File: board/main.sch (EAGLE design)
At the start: 62 parts, among them IC1 W65C02S6TP

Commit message: updated schematic
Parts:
- added IC6: (no value), memory-hitachi:62256P
- added IC7: 74LS00N, 74xx-eu:74LS00N
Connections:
- new net N$58: IC6.!CS, IC7A.O
- new net _A15: IC7A.I1, IC7C.O
- net A0: now also IC6.A0
- net A1: now also IC6.A1
- net A10: now also IC6.A10
- net A11: now also IC6.A11
- net A12: now also IC6.A12
- net A13: now also IC6.A13
- net A14: now also IC6.!OE, IC6.A14
- net A15: now also IC7C.I0, IC7C.I1
- net A2: now also IC6.A2
- net A3: now also IC6.A3
- net A4: now also IC6.A4
- net A5: now also IC6.A5
- net A6: now also IC6.A6
- net A7: now also IC6.A7
- net A8: now also IC6.A8
- net A9: now also IC6.A9
- net CLOCK: now also IC7A.I0
- net D0: now also IC6.I/O0
- net D1: now also IC6.I/O1
- net D2: now also IC6.I/O2
- net D3: now also IC6.I/O3
- net D4: now also IC6.I/O4
- net D5: now also IC6.I/O5
- net D6: now also IC6.I/O6
- net D7: now also IC6.I/O7
- net GND: now also IC6.VSS
- net R/_W: now also IC6.!WE
- net VCC: now also IC6.VCC

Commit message: modified board
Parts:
- added D1, D2: 1N4148DO35-7, diode:1N4148DO35-7
- added D3: 3.9v, diode:ZENER-DIODEDO34-7
- added IC7-ROM: AT28C256-28DIP, atmel-custom:AT28C256-28DIP
- added LED27, LED28: (no value), led:LED5MM
- added Q1: BC327, transistor-pnp:BC327
- added R30, R31: 220Ω, rcl:R-EU_0207/10
- added R32, R33, R34: 220kΩ, rcl:R-EU_0207/10
- added T1: BC337, transistor:BC337
- added U$1: W65C22S6TP, 6502:W65C22S6TP
- renumbered IC6 to IC6-RAM
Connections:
- removed net R/_W: IC11.R!WB, IC5.I7, IC6-RAM.!WE
- removed net _A15: IC7A.I1, IC7C.O
- removed net _RES: C1.1, IC11.!RESB, R1.1, R2.2, S1.P, S1.P1
- new net A14*: IC7A.O, IC7D.I0
- new net A15*: IC7-ROM./OE, IC7C.O, IC7D.I1
- new net CLOCK*: D2.A, IC7-ROM./CE, IC7B.O
- new net CS_RAM: D1.A, IC7D.O, R33.1
- new net N$54: LED27.A, R30.2
- new net N$55: Q1.C, R31.1
- new net N$56: LED28.A, R31.2
- new net N$57: D1.C, D2.C, IC6-RAM.!CS, R32.1
- new net N$59: D3.A, Q1.B
- new net N$60: R34.2, T1.B
- new net N$61: D3.C, R33.2
- new net PB0: U$1VIA.PB0
- new net PB1: U$1VIA.PB1
- new net PB2: U$1VIA.PB2
- new net PB3: U$1VIA.PB3
- new net PB4: U$1VIA.PB4
- new net PB5: U$1VIA.PB5
- new net PB6: U$1VIA.PB6
- new net PB7: U$1VIA.PB7
- new net R/W*: IC11.R!WB, IC5.I7, IC6-RAM.!WE, U$1VIA.R!WB
- new net RES*: C1.1, IC11.!RESB, R1.1, R2.2, S1.P, S1.P1, U$1VIA.!RESB
- net A0: now also IC7-ROM.A0, U$1VIA.RS0
- net A1: now also IC7-ROM.A1, U$1VIA.RS1
- net A10: now also IC7-ROM.A10
- net A11: now also IC7-ROM.A11
- net A12: now also IC7-ROM.A12
- net A13: now also IC7-ROM.A13
- net A14: now also IC7-ROM.A14, IC7A.I0, IC7A.I1, U$1VIA.CS1
- net A15: now also R34.1, U$1VIA.!CS2B
- net A2: now also IC7-ROM.A2, U$1VIA.RS2
- net A3: now also IC7-ROM.A3, U$1VIA.RS3
- net A4: now also IC7-ROM.A4
- net A5: now also IC7-ROM.A5
- net A6: now also IC7-ROM.A6
- net A7: now also IC7-ROM.A7
- net A8: now also IC7-ROM.A8
- net A9: now also IC7-ROM.A9
- net CLOCK: now also IC7B.I0, IC7B.I1, U$1VIA.PHI2; no longer IC7A.I0
- net D0: now also IC7-ROM.I/O0, U$1VIA.D0
- net D1: now also IC7-ROM.I/O1, U$1VIA.D1
- net D2: now also IC7-ROM.I/O2, U$1VIA.D2
- net D3: now also IC7-ROM.I/O3, U$1VIA.D3
- net D4: now also IC7-ROM.I/O4, U$1VIA.D4
- net D5: now also IC7-ROM.I/O5, U$1VIA.D5
- net D6: now also IC7-ROM.I/O6, U$1VIA.D6
- net D7: now also IC7-ROM.I/O7, U$1VIA.D7
- net GND: now also IC7-ROM.GND, IC7P.GND, LED28.C, R32.2, T1.E, U$1VIAP.VSS
- net N$58: now also LED27.C, T1.C; no longer IC6-RAM.!CS, IC7A.O
- net VCC: now also IC7-ROM./WE, IC7-ROM.VCC, IC7P.VCC, Q1.E, R30.1, U$1VIA.!IRQB, U$1VIAP.VDD
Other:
- note added: "CY62256"
- moved on the sheet: IC7A, IC7C

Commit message: modified board
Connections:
- net A15*: now also IC7-ROM./CE; no longer IC7-ROM./OE
- net CLOCK*: no longer IC7-ROM./CE
- net GND: now also IC7-ROM./OE
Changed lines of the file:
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@@
 <part name="GND15" library="supply1" library_urn="urn:adsk.eagle:library:371" deviceset="GND" device=""/>
 <part name="P+13" library="supply1" library_urn="urn:adsk.eagle:library:371" deviceset="VCC" device=""/>
+<part name="GND16" library="supply1" library_urn="urn:adsk.eagle:library:371" deviceset="GND" device=""/>
 </parts>
 <sheets>
@@
 <instance part="P+13" gate="VCC" x="421.64" y="68.58" smashed="yes">
 <attribute name="VALUE" x="419.1" y="66.04" size="1.778" layer="96" rot="R90"/>
+</instance>
+<instance part="GND16" gate="1" x="340.36" y="45.72" smashed="yes">
+<attribute name="VALUE" x="337.82" y="43.18" size="1.778" layer="96"/>
 </instance>
 </instances>
@@
 <pinref part="GND15" gate="1" pin="GND"/>
 </segment>
+<segment>
+<pinref part="IC7-ROM" gate="G$1" pin="/OE"/>
+<wire x1="330.2" y1="50.8" x2="340.36" y2="50.8" width="0.1524" layer="91"/>
+<wire x1="340.36" y1="50.8" x2="340.36" y2="48.26" width="0.1524" layer="91"/>
+<pinref part="GND16" gate="1" pin="GND"/>
+</segment>
 </net>
 <net name="RES*" class="0">
@@
 </segment>
 <segment>
-<pinref part="IC7-ROM" gate="G$1" pin="/OE"/>
-<wire x1="330.2" y1="50.8" x2="332.74" y2="50.8" width="0.1524" layer="91"/>
-<label x="332.74" y="50.8" size="1.27" layer="95" xref="yes"/>
+<label x="332.74" y="48.26" size="1.27" layer="95" xref="yes"/>
+<pinref part="IC7-ROM" gate="G$1" pin="/CE"/>
+<wire x1="332.74" y1="48.26" x2="330.2" y2="48.26" width="0.1524" layer="91"/>
 </segment>
 </net>
@@
 </segment>
 <segment>
-<pinref part="IC7-ROM" gate="G$1" pin="/CE"/>
-<wire x1="330.2" y1="48.26" x2="332.74" y2="48.26" width="0.1524" layer="91"/>
-<label x="332.74" y="48.26" size="1.27" layer="95" xref="yes"/>
-</segment>
-<segment>

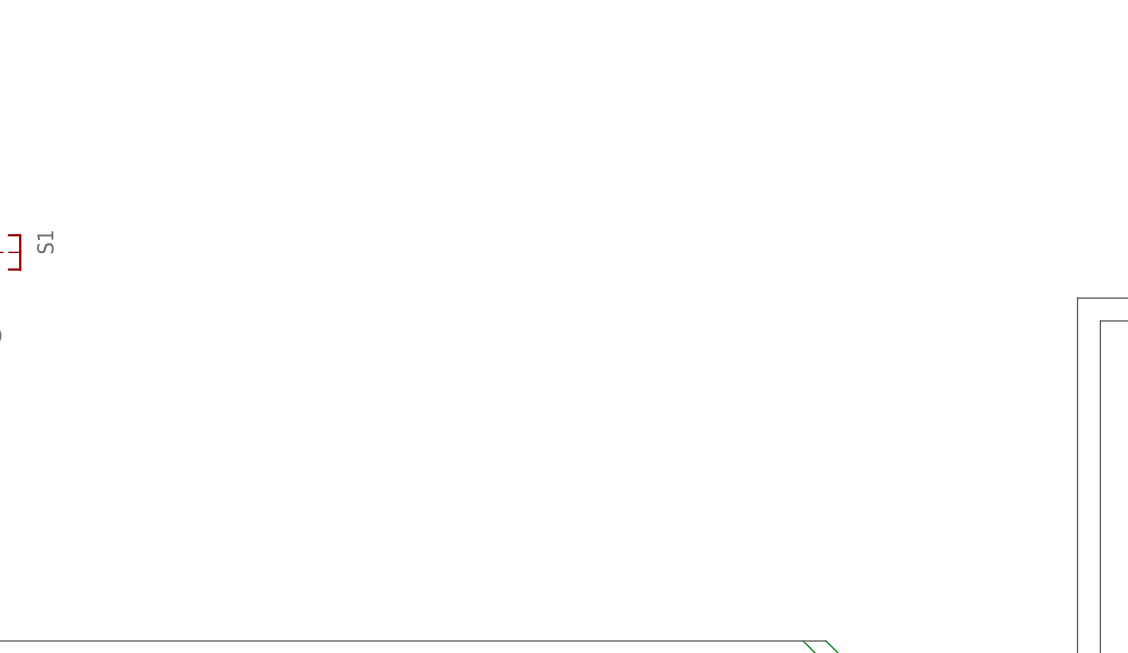
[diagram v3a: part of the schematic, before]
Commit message: added 555 circuit
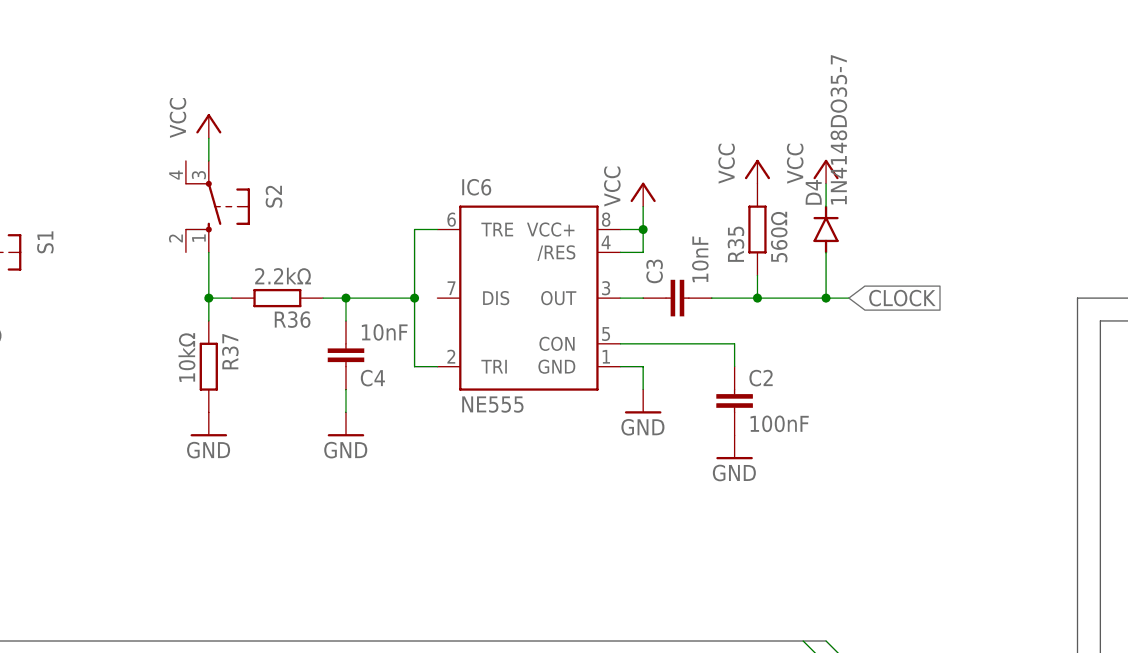
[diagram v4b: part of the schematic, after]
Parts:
- added C2: 100nF, rcl:C-EU050-025X075
- added C3, C4: 10nF, rcl:C-EU050-025X075
- added D4: 1N4148DO35-7, diode:1N4148DO35-7
- added IC6: NE555, st-microelectronics:NE555
- added R35: 560Ω, rcl:R-EU_0207/10
- added R36: 2.2kΩ, rcl:R-EU_0207/10
- added R37: 10kΩ, rcl:R-EU_0207/10
- added S2: (no value), switch-omron:10-XX
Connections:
- new net N$62: C3.1, IC6.OUT
- new net N$63: C4.2, IC6.TRE, IC6.TRI, R36.1
- new net N$64: C2.1, IC6.CON
- new net N$65: R36.2, R37.1, S2.S
- net CLOCK: now also C3.2, D4.A, R35.1
- net GND: now also C2.2, C4.1, IC6.GND, R37.2
- net VCC: now also D4.C, IC6./RES, IC6.VCC+, R35.2, S2.P

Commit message: created ROMImage script in python and added LCD display to the schematic
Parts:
- added DIS1: TUXGR_16X2_R2, display-lcd:TUXGR_16X2_R2
- added R38: 100kΩ, rcl:R-TRIMM64W
- renumbered IC7-ROM to IC8-ROM, U$1 to IC9-PERIPHERALS
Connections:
- new net IRQ*: IC11.!IRQB, IC9-PERIPHERALSVIA.!IRQB
- new net N$66: DIS1.CONTR, R38.S
- new net PA0: DIS1.RS, IC9-PERIPHERALSVIA.PA0
- new net PA1: DIS1.E, IC9-PERIPHERALSVIA.PA1
- new net PA2: IC9-PERIPHERALSVIA.PA2
- new net PA3: IC9-PERIPHERALSVIA.PA3
- new net PA4: DIS1.D4, IC9-PERIPHERALSVIA.PA4
- new net PA5: DIS1.D5, IC9-PERIPHERALSVIA.PA5
- new net PA6: DIS1.D6, IC9-PERIPHERALSVIA.PA6
- new net PA7: DIS1.D7, IC9-PERIPHERALSVIA.PA7
- net GND: now also DIS1.GND, DIS1.NC@2, R38.A
- net R/W*: now also DIS1.R/W
- net VCC: now also DIS1.NC@1, DIS1.VCC, R38.E; no longer IC11.!IRQB, IC9-PERIPHERALSVIA.!IRQB
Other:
- note added: "A"
- note added: "K"
- moved on the sheet: R3

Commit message: varius things
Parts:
- R38: value 100kΩ -> 10kΩ
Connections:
- net PA1: now also DIS1.R/W; no longer DIS1.E
- net PA2: now also DIS1.E
- net R/W*: no longer DIS1.R/W
- net VCC: no longer R38.E
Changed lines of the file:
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@@
 <part name="GND21" library="supply1" library_urn="urn:adsk.eagle:library:371" deviceset="GND" device=""/>
 <part name="P+13" library="supply1" library_urn="urn:adsk.eagle:library:371" deviceset="VCC" device=""/>
-<part name="R38" library="rcl" library_urn="urn:adsk.eagle:library:334" deviceset="R-TRIMM" device="64W" package3d_urn="urn:adsk.eagle:package:23748/1" value="100kΩ"/>
+<part name="R38" library="rcl" library_urn="urn:adsk.eagle:library:334" deviceset="R-TRIMM" device="64W" package3d_urn="urn:adsk.eagle:package:23748/1" value="10kΩ"/>
 <part name="P+18" library="supply1" library_urn="urn:adsk.eagle:library:371" deviceset="VCC" device=""/>
 <part name="GND22" library="supply1" library_urn="urn:adsk.eagle:library:371" deviceset="GND" device=""/>
@@
 </instance>
 <instance part="IC9-PERIPHERALS" gate="VIA" x="393.7" y="50.8" smashed="yes">
-<attribute name="PART" x="389.255" y="80.645" size="1.778" layer="95"/>
+<attribute name="PART" x="384.175" y="80.645" size="1.778" layer="95"/>
 <attribute name="VALUE" x="386.715" y="19.05" size="1.778" layer="96"/>
 </instance>
@@
 <attribute name="VALUE" x="434.34" y="58.42" size="1.778" layer="96"/>
 </instance>
-<instance part="P+13" gate="VCC" x="436.88" y="88.9" smashed="yes">
-<attribute name="VALUE" x="434.34" y="86.36" size="1.778" layer="96" rot="R90"/>
+<instance part="P+13" gate="VCC" x="447.04" y="88.9" smashed="yes">
+<attribute name="VALUE" x="444.5" y="86.36" size="1.778" layer="96" rot="R90"/>
 </instance>
 <instance part="R38" gate="G$1" x="436.88" y="73.66" smashed="yes">
@@
 </segment>
 <segment>
-<pinref part="R38" gate="G$1" pin="E"/>
 <pinref part="P+13" gate="VCC" pin="VCC"/>
-<wire x1="436.88" y1="86.36" x2="436.88" y2="81.28" width="0.1524" layer="91"/>
 <pinref part="DIS1" gate="G$1" pin="VCC"/>
-<wire x1="436.88" y1="81.28" x2="436.88" y2="78.74" width="0.1524" layer="91"/>
 <wire x1="454.66" y1="76.2" x2="447.04" y2="76.2" width="0.1524" layer="91"/>
-<wire x1="447.04" y1="76.2" x2="447.04" y2="81.28" width="0.1524" layer="91"/>
-<wire x1="447.04" y1="81.28" x2="436.88" y2="81.28" width="0.1524" layer="91"/>
-<junction x="436.88" y="81.28"/>
+<wire x1="447.04" y1="76.2" x2="447.04" y2="86.36" width="0.1524" layer="91"/>
 </segment>
 <segment>
@@
 <label x="220.98" y="35.56" size="1.27" layer="95" rot="R180" xref="yes"/>
 </segment>
-<segment>
-<pinref part="DIS1" gate="G$1" pin="R/W"/>
-<wire x1="454.66" y1="68.58" x2="452.12" y2="68.58" width="0.1524" layer="91"/>
-<label x="452.12" y="68.58" size="1.27" layer="95" rot="R180" xref="yes"/>
-</segment>
 </net>
 <net name="PB0" class="0">
@@
 <net name="PA1" class="0">
 <segment>
+<pinref part="IC9-PERIPHERALS" gate="VIA" pin="PA1"/>
+<wire x1="381" y1="73.66" x2="378.46" y2="73.66" width="0.1524" layer="91"/>
+<label x="378.46" y="73.66" size="1.27" layer="95" rot="R180" xref="yes"/>
+</segment>
+<segment>
+<pinref part="DIS1" gate="G$1" pin="R/W"/>
+<wire x1="454.66" y1="68.58" x2="452.12" y2="68.58" width="0.1524" layer="91"/>
+<label x="452.12" y="68.58" size="1.27" layer="95" rot="R180" xref="yes"/>
+</segment>
+</net>
+<net name="PA0" class="0">
+<segment>
+<pinref part="DIS1" gate="G$1" pin="RS"/>
+<wire x1="454.66" y1="71.12" x2="452.12" y2="71.12" width="0.1524" layer="91"/>
+<label x="452.12" y="71.12" size="1.27" layer="95" rot="R180" xref="yes"/>
+</segment>
+<segment>
+<pinref part="IC9-PERIPHERALS" gate="VIA" pin="PA0"/>
+<wire x1="381" y1="76.2" x2="378.46" y2="76.2" width="0.1524" layer="91"/>
+<label x="378.46" y="76.2" size="1.27" layer="95" rot="R180" xref="yes"/>
+</segment>
+</net>
+<net name="N$66" class="0">
+<segment>
+<pinref part="DIS1" gate="G$1" pin="CONTR"/>
+<pinref part="R38" gate="G$1" pin="S"/>
+<wire x1="454.66" y1="73.66" x2="441.96" y2="73.66" width="0.1524" layer="91"/>
+</segment>
+</net>
+<net name="PA2" class="0">
+<segment>
+<pinref part="IC9-PERIPHERALS" gate="VIA" pin="PA2"/>
+<wire x1="381" y1="71.12" x2="378.46" y2="71.12" width="0.1524" layer="91"/>
+<label x="378.46" y="71.12" size="1.27" layer="95" rot="R180" xref="yes"/>
+</segment>
+<segment>
 <pinref part="DIS1" gate="G$1" pin="E"/>
 <wire x1="454.66" y1="66.04" x2="452.12" y2="66.04" width="0.1524" layer="91"/>
 <label x="452.12" y="66.04" size="1.27" layer="95" rot="R180" xref="yes"/>
 </segment>
-<segment>
-<pinref part="IC9-PERIPHERALS" gate="VIA" pin="PA1"/>
-<wire x1="381" y1="73.66" x2="378.46" y2="73.66" width="0.1524" layer="91"/>
-<label x="378.46" y="73.66" size="1.27" layer="95" rot="R180" xref="yes"/>
-</segment>
-</net>
-<net name="PA0" class="0">
-<segment>
-<pinref part="DIS1" gate="G$1" pin="RS"/>
-<wire x1="454.66" y1="71.12" x2="452.12" y2="71.12" width="0.1524" layer="91"/>
-<label x="452.12" y="71.12" size="1.27" layer="95" rot="R180" xref="yes"/>
-</segment>
-<segment>
-<pinref part="IC9-PERIPHERALS" gate="VIA" pin="PA0"/>
-<wire x1="381" y1="76.2" x2="378.46" y2="76.2" width="0.1524" layer="91"/>
-<label x="378.46" y="76.2" size="1.27" layer="95" rot="R180" xref="yes"/>
-</segment>
-</net>
-<net name="N$66" class="0">
-<segment>
-<pinref part="DIS1" gate="G$1" pin="CONTR"/>
-<pinref part="R38" gate="G$1" pin="S"/>
-<wire x1="454.66" y1="73.66" x2="441.96" y2="73.66" width="0.1524" layer="91"/>
-</segment>
-</net>
-<net name="PA2" class="0">
-<segment>
-<pinref part="IC9-PERIPHERALS" gate="VIA" pin="PA2"/>
-<wire x1="381" y1="71.12" x2="378.46" y2="71.12" width="0.1524" layer="91"/>
-<label x="378.46" y="71.12" size="1.27" layer="95" rot="R180" xref="yes"/>
-</segment>
-</net>
+</net>

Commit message: added lcd
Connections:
- net PA3: now also DIS1.NC@1
- net VCC: no longer DIS1.NC@1
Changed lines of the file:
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@@
 <part name="P+13" library="supply1" library_urn="urn:adsk.eagle:library:371" deviceset="VCC" device=""/>
 <part name="R38" library="rcl" library_urn="urn:adsk.eagle:library:334" deviceset="R-TRIMM" device="64W" package3d_urn="urn:adsk.eagle:package:23748/1" value="10kΩ"/>
-<part name="P+18" library="supply1" library_urn="urn:adsk.eagle:library:371" deviceset="VCC" device=""/>
 <part name="GND22" library="supply1" library_urn="urn:adsk.eagle:library:371" deviceset="GND" device=""/>
 </parts>
@@
 <attribute name="VALUE" x="433.07" y="69.85" size="1.778" layer="96" rot="R90"/>
 </instance>
-<instance part="P+18" gate="VCC" x="441.96" y="48.26" smashed="yes">
-<attribute name="VALUE" x="439.42" y="45.72" size="1.778" layer="96" rot="R90"/>
-</instance>
-<instance part="GND22" gate="1" x="441.96" y="35.56" smashed="yes">
-<attribute name="VALUE" x="439.42" y="33.02" size="1.778" layer="96"/>
+<instance part="GND22" gate="1" x="452.12" y="35.56" smashed="yes">
+<attribute name="VALUE" x="449.58" y="33.02" size="1.778" layer="96"/>
 </instance>
 </instances>
@@
 <wire x1="447.04" y1="76.2" x2="447.04" y2="86.36" width="0.1524" layer="91"/>
 </segment>
-<segment>
-<pinref part="P+18" gate="VCC" pin="VCC"/>
-<wire x1="441.96" y1="45.72" x2="441.96" y2="43.18" width="0.1524" layer="91"/>
-<pinref part="DIS1" gate="G$1" pin="NC@1"/>
-<wire x1="441.96" y1="43.18" x2="454.66" y2="43.18" width="0.1524" layer="91"/>
-</segment>
 </net>
 <net name="GND" class="0">
@@
 </segment>
 <segment>
+<pinref part="GND22" gate="1" pin="GND"/>
+<wire x1="452.12" y1="40.64" x2="452.12" y2="38.1" width="0.1524" layer="91"/>
 <pinref part="DIS1" gate="G$1" pin="NC@2"/>
-<wire x1="454.66" y1="40.64" x2="441.96" y2="40.64" width="0.1524" layer="91"/>
-<pinref part="GND22" gate="1" pin="GND"/>
-<wire x1="441.96" y1="40.64" x2="441.96" y2="38.1" width="0.1524" layer="91"/>
+<wire x1="454.66" y1="40.64" x2="452.12" y2="40.64" width="0.1524" layer="91"/>
 </segment>
 </net>
@@
 <label x="378.46" y="68.58" size="1.27" layer="95" rot="R180" xref="yes"/>
 </segment>
-</net>
+<segment>
+<pinref part="DIS1" gate="G$1" pin="NC@1"/>
+<wire x1="454.66" y1="43.18" x2="452.12" y2="43.18" width="0.1524" layer="91"/>
+<label x="452.12" y="43.18" size="1.27" layer="95" rot="R180" xref="yes"/>
+</segment>
+</net>

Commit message: ciao
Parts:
- added Q2, Q3: BC327, transistor-pnp:BC327
- added R39, R41: 1kΩ, rcl:R-EU_0207/10
- added R40, R42: 10kΩ, rcl:R-EU_0207/10
- C4: value 10nF -> 10uF
- R32: value 220kΩ -> 10kΩ
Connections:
- new net N$67: IC6-RAM.!CS, IC7B.O
- new net N$68: Q2.B, R39.2
- new net N$69: Q2.C, R40.1, R41.1
- new net N$70: Q3.B, R41.2
- new net N$71: Q3.C, R42.1
- net A15*: now also IC7B.I1
- net CLOCK: no longer IC7B.I1
- net CLOCK*: no longer IC7B.O
- net GND: now also R40.2, R42.2
- net N$57: now also R39.1; no longer IC6-RAM.!CS
- net VCC: now also Q2.E, Q3.E
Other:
- moved on the sheet: D1, D2, R32
